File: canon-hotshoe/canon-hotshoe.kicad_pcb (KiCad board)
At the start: 2 copper layers, 18 x 18 mm, 11 parts, among them J1 PogoPin, J10 PogoPin, J11 PogoPin, J2 PogoPin, J3 PogoPin, J4 PogoPin, J5 PogoPin, J6 PogoPin, J7 PogoPin, J8 PogoPin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

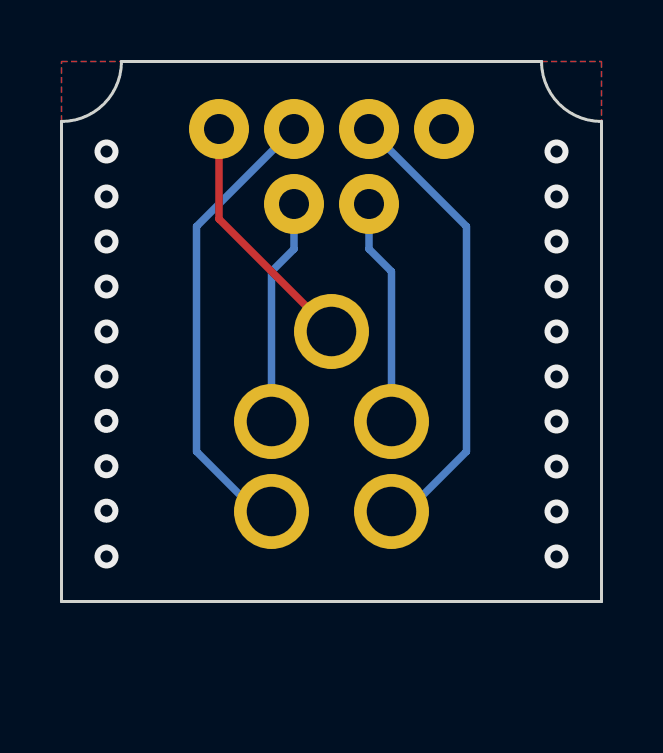
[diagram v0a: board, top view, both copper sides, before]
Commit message: Fixes and improvements
 * fix the preflash detection
 * clean the canon hot shoe schematics up
 * enlarge the hotshoe pcb and place two new mounting pins
 * change the battery low to a battery good detection
 * move the supervisor ic away from the hot shoe rail
 * use a longer pogo pin
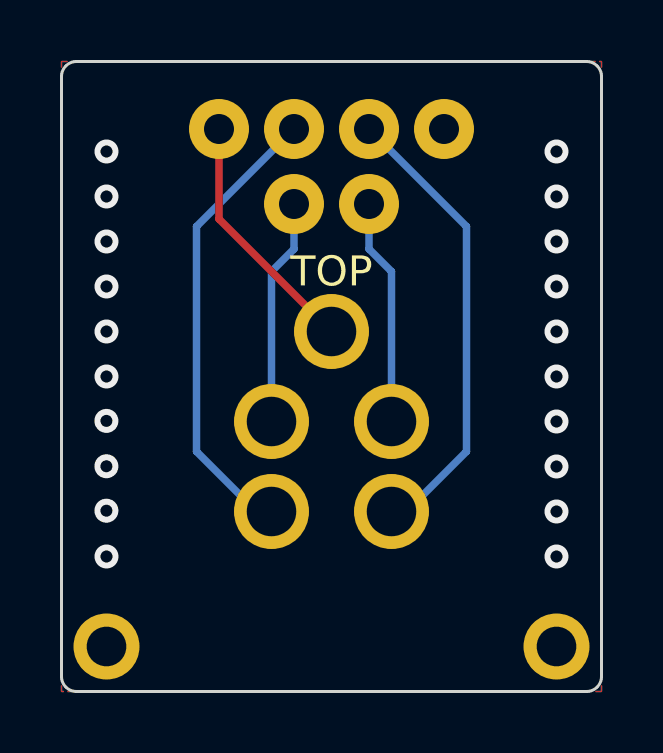
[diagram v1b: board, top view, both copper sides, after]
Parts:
- added J2: 0550, Connector_MillMax:0550_52mil, F.Cu at (145.5, 110.5)
- added J3: 0550, Connector_MillMax:0550_52mil, F.Cu at (160.5, 110.5)
- J1: value PogoPin -> 0900-0; footprint Connector_MillMax:0965_1.65mm_Reverse -> Connector_MillMax:0900-0_137mil_Reverse
- J10: renamed from J5; value PogoPin -> 0508
- J11: renamed from J3; value PogoPin -> 0508
- J12: renamed from J11; value PogoPin -> 0508
- J13: renamed from J2; value PogoPin -> 0508
- J4: renamed from J9; value PogoPin -> 0508
- J5: renamed from J7; value PogoPin -> 0508
- J6: renamed from J4; value PogoPin -> 0900-0; footprint Connector_MillMax:0965_1.65mm_Reverse -> Connector_MillMax:0900-0_137mil_Reverse
- J7: renamed from J10; value PogoPin -> 0900-0; footprint Connector_MillMax:0965_1.65mm_Reverse -> Connector_MillMax:0900-0_137mil_Reverse
- J8: renamed from J6; value PogoPin -> 0900-0; footprint Connector_MillMax:0965_1.65mm_Reverse -> Connector_MillMax:0900-0_137mil_Reverse
- J9: renamed from J8; value PogoPin -> 0900-0; footprint Connector_MillMax:0965_1.65mm_Reverse -> Connector_MillMax:0900-0_137mil_Reverse
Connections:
- net Net-(J1-Pad1) renamed /X
- net Net-(J10-Pad1) renamed /EFID0
- net Net-(J11-Pad1) renamed /AVEFI
- net Net-(J2-Pad1) renamed /CCC
- net Net-(J4-Pad1) renamed /STSPC
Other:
- board size 18 x 18 mm -> 18 x 21 mm
- board text added: "TOP"

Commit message: Renumber RefDes and add OSHW logo and URL
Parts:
- added REF**: OSHW-Symbol_4x4.6mm_SilkScreen, Symbol_Own:OSHW-Symbol_4x4.6mm_SilkScreen, B.Cu at (153.0, 110.2)
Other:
- board text added: "github.com/mwalle/flash-trigger"
- board text added: "rev2"

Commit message: canon-hotshoe: exclude OSHW symbol from schematics
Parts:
- renumbered REF** to ?
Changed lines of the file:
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@@
     (descr "Open Source Hardware Logo")
     (tags "Logo OSHW")
-    (attr exclude_from_pos_files exclude_from_bom)
-    (fp_text reference "REF**" (at 0 0) (layer "B.SilkS") hide
+    (attr board_only exclude_from_pos_files exclude_from_bom)
+    (fp_text reference "" (at 0 0) (layer "B.SilkS") hide
       (effects (font (size 1 1) (thickness 0.15)) (justify mirror))
     )
